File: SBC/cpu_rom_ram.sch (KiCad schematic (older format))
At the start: 6 parts, among them U1 WD65C02PLCC44, U2 28C256, U3 AS6C62256A

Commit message: Preparation for Pluto v3.0
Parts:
- removed U2: 28C256, Housings_DIP:DIP-28_W15.24mm_Socket, symbol pluto-rescue:28C256-RESCUE-pluto
- added U2: AT28HC256EPLCC32, Grotto:PLCC-32_THT-Socket, symbol Grotto:AT28HC256EPLCC32
- C1, C2, C3: footprint Capacitors_ThroughHole:C_Disc_D4.7mm_W2.5mm_P5.00mm -> Capacitor_THT:C_Disc_D4.7mm_W2.5mm_P5.00mm
- U1: symbol 65xx:WD65C02PLCC44 -> pluto-rescue:WD65C02PLCC44-65xx
- U3: footprint Housings_DIP:DIP-28_W15.24mm_Socket -> Package_DIP:DIP-28_W7.62mm_Socket
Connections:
- net labels added: R-~W
- net labels removed: R/~W
- wire segments 99 -> 100
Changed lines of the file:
@@
 EESchema Schematic File Version 4
 LIBS:pluto-cache
-EELAYER 29 0
+EELAYER 30 0
 EELAYER END
 $Descr A4 11693 8268
@@
 F 0 "C1" V 2250 4125 50  0000 L CNN
 F 1 "0.1uF" V 2250 3750 50  0000 L CNN
-F 2 "Capacitors_ThroughHole:C_Disc_D4.7mm_W2.5mm_P5.00mm" H 2213 3875 50  0001 C CNN
+F 2 "Capacitor_THT:C_Disc_D4.7mm_W2.5mm_P5.00mm" H 2213 3875 50  0001 C CNN
 F 3 "" H 2175 4025 50  0001 C CNN
 	1    2175 4025
@@
 F 0 "C2" H 5800 3800 50  0000 L CNN
 F 1 "0.1uF" H 5800 3600 50  0000 L CNN
-F 2 "Capacitors_ThroughHole:C_Disc_D4.7mm_W2.5mm_P5.00mm" H 5813 3550 50  0001 C CNN
+F 2 "Capacitor_THT:C_Disc_D4.7mm_W2.5mm_P5.00mm" H 5813 3550 50  0001 C CNN
 F 3 "" H 5775 3700 50  0001 C CNN
 	1    5775 3700
@@
 L power:VCC #PWR02
 U 1 1 5924D609
-P 2825 3450
-F 0 "#PWR02" H 2825 3300 50  0001 C CNN
-F 1 "VCC" V 2825 3650 50  0000 C CNN
-F 2 "" H 2825 3450 50  0001 C CNN
-F 3 "" H 2825 3450 50  0001 C CNN
-	1    2825 3450
+P 2950 3450
+F 0 "#PWR02" H 2950 3300 50  0001 C CNN
+F 1 "VCC" V 2950 3650 50  0000 C CNN
+F 2 "" H 2950 3450 50  0001 C CNN
+F 3 "" H 2950 3450 50  0001 C CNN
+	1    2950 3450
 	0    1    1    0
 $EndComp
@@
 ~IRQ
 Text HLabel 1300 2950 0    60   Output ~ 0
-R/~W
+R-~W
 Text HLabel 1300 3050 0    60   Input ~ 0
 ~NMI
@@
 ~ROMSEL
 $Comp
-L pluto-rescue:28C256-RESCUE-pluto U2
-U 1 1 59386D85
-P 5775 2300
-F 0 "U2" H 5975 3300 50  0000 C CNN
-F 1 "28C256" H 6075 1300 50  0000 C CNN
-F 2 "Housings_DIP:DIP-28_W15.24mm_Socket" H 5775 2300 50  0001 C CNN
-F 3 "" H 5775 2300 50  0001 C CNN
-	1    5775 2300
-	1    0    0    -1
-$EndComp
-$Comp
 L pluto:AS6C62256A U3
 U 1 1 59399129
@@
 F 0 "U3" H 8575 3100 60  0000 C CNN
 F 1 "AS6C62256A" V 8450 2250 60  0000 C CNN
-F 2 "Housings_DIP:DIP-28_W15.24mm_Socket" H 8450 2225 60  0001 C CNN
+F 2 "Package_DIP:DIP-28_W7.62mm_Socket" H 8450 2225 60  0001 C CNN
 F 3 "" H 8450 2225 60  0001 C CNN
 	1    8450 2225
@@
 F 0 "C3" H 8475 3650 50  0000 L CNN
 F 1 "0.1uF" H 8475 3450 50  0000 L CNN
-F 2 "Capacitors_ThroughHole:C_Disc_D4.7mm_W2.5mm_P5.00mm" H 8488 3400 50  0001 C CNN
+F 2 "Capacitor_THT:C_Disc_D4.7mm_W2.5mm_P5.00mm" H 8488 3400 50  0001 C CNN
 F 3 "" H 8450 3550 50  0001 C CNN
 	1    8450 3550
@@
 ~SO
 $Comp
-L 65xx:WD65C02PLCC44 U1
+L pluto-rescue:WD65C02PLCC44-65xx U1
 U 1 1 59EBAA82
 P 2175 2600
+AR Path="/59EBAA82" Ref="U1"  Part="1"
+AR Path="/58D5892B/59EBAA82" Ref="U1"  Part="1"
 F 0 "U1" H 2175 1450 60  0000 C CNN
 F 1 "WD65C02PLCC44" V 2175 2650 60  0000 C CNN
@@
 Wire Wire Line
 	2825 3550 2825 4025
+Wire Wire Line
+	2825 3450 2950 3450
+Connection ~ 2825 3450
+$Comp
+L Grotto:AT28HC256EPLCC32 U2
+U 1 1 5D81EA08
+P 5775 2300
+F 0 "U2" H 5775 3731 50  0000 C CNN
+F 1 "AT28HC256EPLCC32" V 5775 2350 50  0000 C CNN
+F 2 "Grotto:PLCC-32_THT-Socket" H 5775 2300 50  0001 C CNN
+F 3 "" H 5775 2300 50  0001 C CNN
+	1    5775 2300
+	1    0    0    -1
+$EndComp
+Connection ~ 5775 3550
+Connection ~ 5775 1050
 Wire Bus Line
 	1200 725  1200 2050

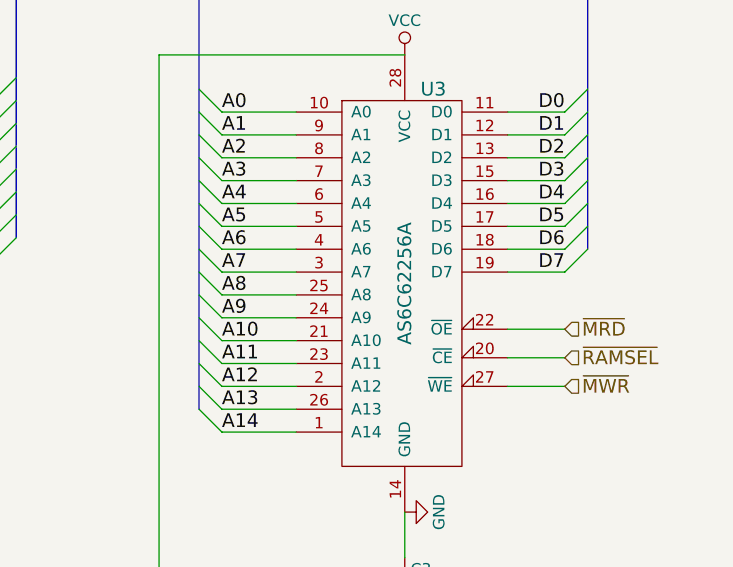
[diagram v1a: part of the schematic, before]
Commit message: Converting to SMD of almost all components.
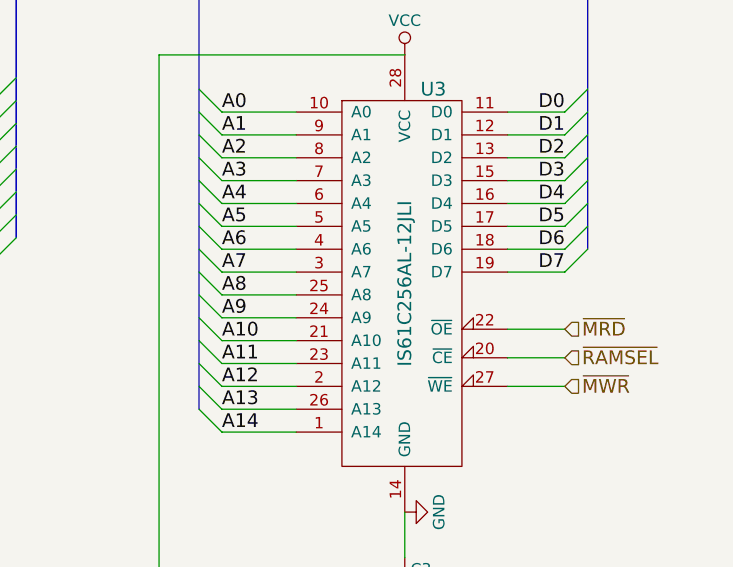
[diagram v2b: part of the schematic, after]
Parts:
- C1, C2, C3: footprint Capacitor_THT:C_Disc_D4.7mm_W2.5mm_P5.00mm -> Capacitor_SMD:C_0603_1608Metric_Pad1.05x0.95mm_HandSolder
- U3: value AS6C62256A -> IS61C256AL-12JLI; footprint Package_DIP:DIP-28_W7.62mm_Socket -> Package_SO:SSOP-28_3.9x9.9mm_P0.635mm
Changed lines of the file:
@@
 F 0 "C1" V 2250 4125 50  0000 L CNN
 F 1 "0.1uF" V 2250 3750 50  0000 L CNN
-F 2 "Capacitor_THT:C_Disc_D4.7mm_W2.5mm_P5.00mm" H 2213 3875 50  0001 C CNN
+F 2 "Capacitor_SMD:C_0603_1608Metric_Pad1.05x0.95mm_HandSolder" H 2213 3875 50  0001 C CNN
 F 3 "" H 2175 4025 50  0001 C CNN
 	1    2175 4025
@@
 F 0 "C2" H 5800 3800 50  0000 L CNN
 F 1 "0.1uF" H 5800 3600 50  0000 L CNN
-F 2 "Capacitor_THT:C_Disc_D4.7mm_W2.5mm_P5.00mm" H 5813 3550 50  0001 C CNN
+F 2 "Capacitor_SMD:C_0603_1608Metric_Pad1.05x0.95mm_HandSolder" H 5813 3550 50  0001 C CNN
 F 3 "" H 5775 3700 50  0001 C CNN
 	1    5775 3700
@@
 P 8450 2225
 F 0 "U3" H 8575 3100 60  0000 C CNN
-F 1 "AS6C62256A" V 8450 2250 60  0000 C CNN
-F 2 "Package_DIP:DIP-28_W7.62mm_Socket" H 8450 2225 60  0001 C CNN
+F 1 "IS61C256AL-12JLI" V 8450 2250 60  0000 C CNN
+F 2 "Package_SO:SSOP-28_3.9x9.9mm_P0.635mm" H 8450 2225 60  0001 C CNN
 F 3 "" H 8450 2225 60  0001 C CNN
 	1    8450 2225
@@
 F 0 "C3" H 8475 3650 50  0000 L CNN
 F 1 "0.1uF" H 8475 3450 50  0000 L CNN
-F 2 "Capacitor_THT:C_Disc_D4.7mm_W2.5mm_P5.00mm" H 8488 3400 50  0001 C CNN
+F 2 "Capacitor_SMD:C_0603_1608Metric_Pad1.05x0.95mm_HandSolder" H 8488 3400 50  0001 C CNN
 F 3 "" H 8450 3550 50  0001 C CNN
 	1    8450 3550

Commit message: New PCB layout is taking shape.
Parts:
- C1, C2, C3: footprint Capacitor_SMD:C_0603_1608Metric_Pad1.05x0.95mm_HandSolder -> Capacitor_SMD:C_0805_2012Metric_Pad1.15x1.40mm_HandSolder
- U3: footprint Package_SO:SSOP-28_3.9x9.9mm_P0.635mm -> Package_SO:SOJ-28_7.585x18.12mm_P1.27mm
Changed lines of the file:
@@
 F 0 "C1" V 2250 4125 50  0000 L CNN
 F 1 "0.1uF" V 2250 3750 50  0000 L CNN
-F 2 "Capacitor_SMD:C_0603_1608Metric_Pad1.05x0.95mm_HandSolder" H 2213 3875 50  0001 C CNN
+F 2 "Capacitor_SMD:C_0805_2012Metric_Pad1.15x1.40mm_HandSolder" H 2213 3875 50  0001 C CNN
 F 3 "" H 2175 4025 50  0001 C CNN
 	1    2175 4025
@@
 F 0 "C2" H 5800 3800 50  0000 L CNN
 F 1 "0.1uF" H 5800 3600 50  0000 L CNN
-F 2 "Capacitor_SMD:C_0603_1608Metric_Pad1.05x0.95mm_HandSolder" H 5813 3550 50  0001 C CNN
+F 2 "Capacitor_SMD:C_0805_2012Metric_Pad1.15x1.40mm_HandSolder" H 5813 3550 50  0001 C CNN
 F 3 "" H 5775 3700 50  0001 C CNN
 	1    5775 3700
@@
 F 0 "U3" H 8575 3100 60  0000 C CNN
 F 1 "IS61C256AL-12JLI" V 8450 2250 60  0000 C CNN
-F 2 "Package_SO:SSOP-28_3.9x9.9mm_P0.635mm" H 8450 2225 60  0001 C CNN
+F 2 "Package_SO:SOJ-28_7.585x18.12mm_P1.27mm" H 8450 2225 60  0001 C CNN
 F 3 "" H 8450 2225 60  0001 C CNN
 	1    8450 2225
@@
 F 0 "C3" H 8475 3650 50  0000 L CNN
 F 1 "0.1uF" H 8475 3450 50  0000 L CNN
-F 2 "Capacitor_SMD:C_0603_1608Metric_Pad1.05x0.95mm_HandSolder" H 8488 3400 50  0001 C CNN
+F 2 "Capacitor_SMD:C_0805_2012Metric_Pad1.15x1.40mm_HandSolder" H 8488 3400 50  0001 C CNN
 F 3 "" H 8450 3550 50  0001 C CNN
 	1    8450 3550

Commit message: Added de-coupling cap to 74hc74. Rearranged PCB a bit.
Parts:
- U3: footprint Package_SO:SOJ-28_7.585x18.12mm_P1.27mm -> Grotto:SOJ-28_7.585x18.12mm_P1.27mm
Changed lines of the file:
@@
 F 0 "U3" H 8575 3100 60  0000 C CNN
 F 1 "IS61C256AL-12JLI" V 8450 2250 60  0000 C CNN
-F 2 "Package_SO:SOJ-28_7.585x18.12mm_P1.27mm" H 8450 2225 60  0001 C CNN
+F 2 "Grotto:SOJ-28_7.585x18.12mm_P1.27mm" H 8450 2225 60  0001 C CNN
 F 3 "" H 8450 2225 60  0001 C CNN
 	1    8450 2225
